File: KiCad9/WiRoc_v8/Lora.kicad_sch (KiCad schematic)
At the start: 11 parts, among them J11 Conn_01x05, J7 Conn_02x05_Odd_Even, J9 Conn_Coaxial, U8 RAK3172-xx-43-SM-xI

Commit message: etc
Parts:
- removed C18: 4.7uF, Capacitor_SMD:C_0402_1005Metric, symbol Device:C
- added C15, C21: 47uF, Capacitor_SMD:C_1206_3216Metric, symbol Device:C
- added FB1: FerriteBead, Capacitor_SMD:C_1206_3216Metric, symbol Device:FerriteBead
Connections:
- net GND: now also C15.2, C21.2
- net VDD_SYS_3.3V: now also C15.1, FB1.1; no longer U8.24 (VDD)
- new net: C21.1, FB1.2, U8.24 (VDD)
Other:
- note added: "NOTES...Ferrite bead for 1.5Mhz supply switching, 440Mhz radio: muRata BLM31PG601SN1L Or TDK MPZ2012S601AT000 https://www.youtube.com/watch?v=S6Uxx5PCRQY https://www.youtube.com/watch?v=TpXvac1Y3h0"
- moved on the sheet: R59

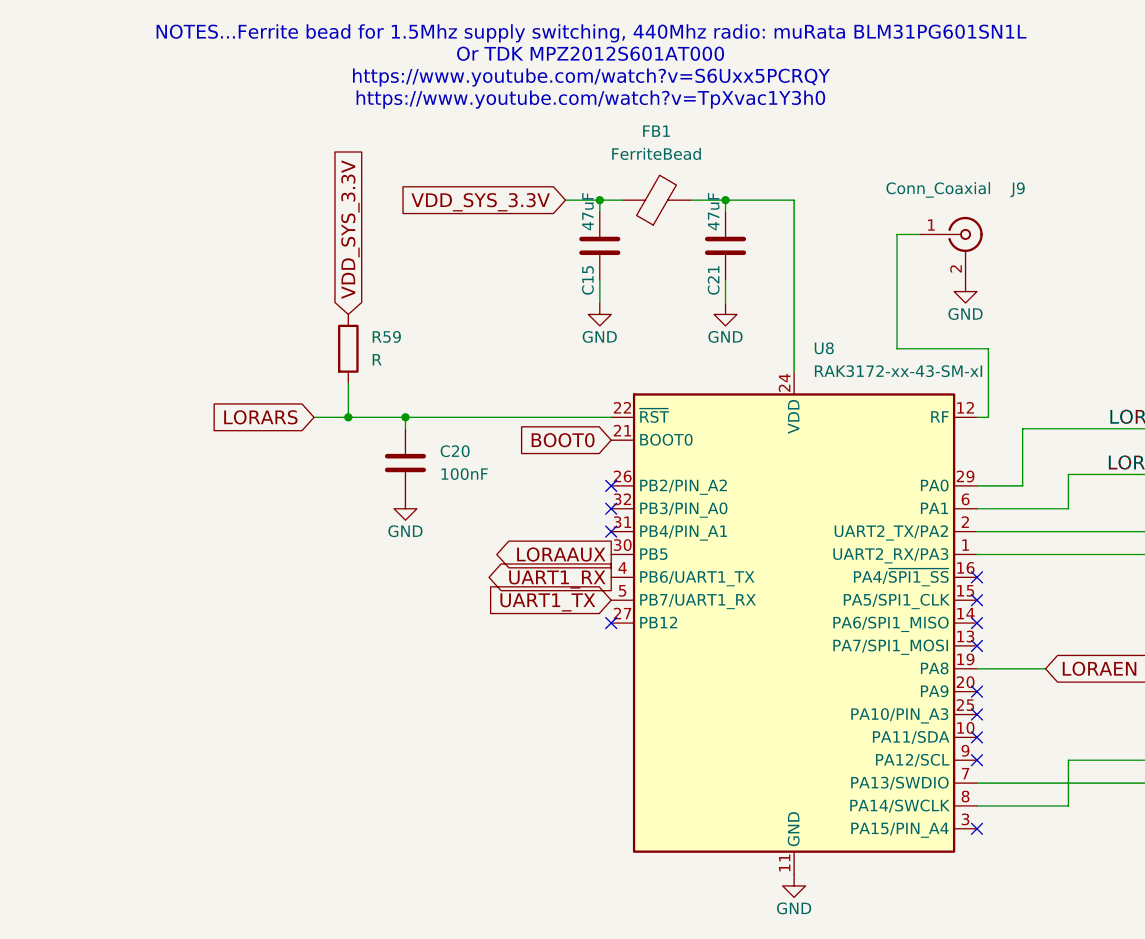
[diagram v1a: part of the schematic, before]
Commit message: add bom
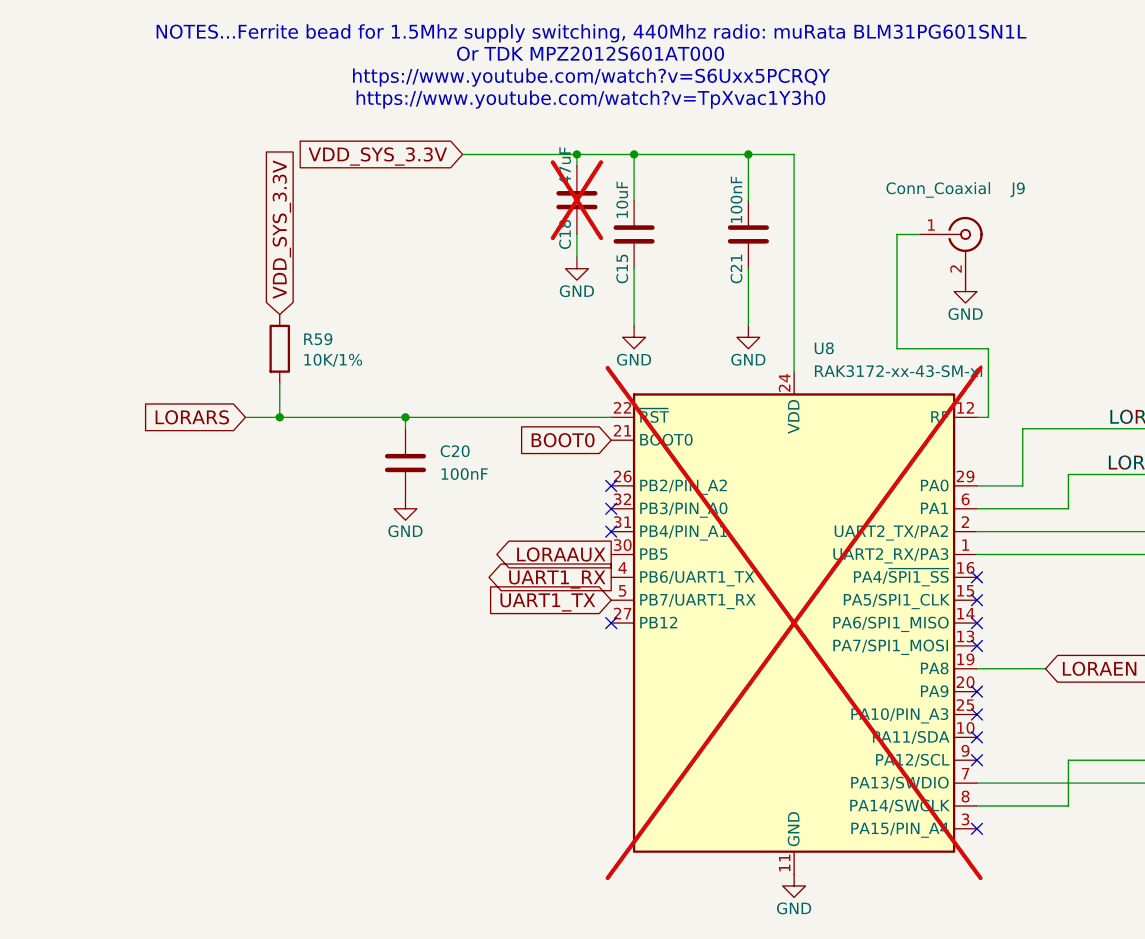
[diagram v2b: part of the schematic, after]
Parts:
- removed FB1: FerriteBead, Capacitor_SMD:C_1206_3216Metric, symbol Device:FerriteBead
- added C18: 47uF, Capacitor_SMD:C_1206_3216Metric, symbol Device:C
- C15: value 47uF -> 10uF; footprint Capacitor_SMD:C_1206_3216Metric -> Capacitor_SMD:C_0402_1005Metric; JLCBasicExtended (none) -> Basic; LCSC Part # C96123 -> C15525; Manufacturer Murata Electronics -> Samsung Electro-Mechanics; ManufacturerPartNumber CL31A476MPHNNNE -> CL05A106MQ5NUNC; Package 1206 -> 0402
- C20: IncludeInBOM (none) -> TRUE; JLCBasicExtended (none) -> Basic; LCSC Part # (none) -> C1525; Manufacturer (none) -> Samsung Electro-Mechanics; ManufacturerPartNumber (none) -> CL05B104KO5NNNC; Package (none) -> 0402
- C21: value 47uF -> 100nF; footprint Capacitor_SMD:C_1206_3216Metric -> Capacitor_SMD:C_0402_1005Metric; JLCBasicExtended (none) -> Basic; LCSC Part # C96123 -> C1525; Manufacturer Murata Electronics -> Samsung Electro-Mechanics; ManufacturerPartNumber CL31A476MPHNNNE -> CL05B104KO5NNNC; Package 1206 -> 0402
- D3: JLCBasicExtended (none) -> Extended
- J11: IncludeInBOM (none) -> FALSE; JLCBasicExtended (none) -> Extended; LCSC Part # (none) -> C6332198; Manufacturer (none) -> Hanbo Electronic; ManufacturerPartNumber (none) -> HB-PH3-25415PB2GOP
- J7: IncludeInBOM (none) -> FALSE; JLCBasicExtended (none) -> Extended; LCSC Part # (none) -> C5142394; Manufacturer (none) -> MINTRON; ManufacturerPartNumber (none) -> MTP310-1205S2
- R56, R57, R58: JLCBasicExtended (none) -> Basic; LCSC Part # C21190 -> C11702; ManufacturerPartNumber 0603WAJ0102T5E -> 0402WGF1001TCE; Package 0603 -> 0402
- R59: value R -> 10K/1%; IncludeInBOM (none) -> TRUE; JLCBasicExtended (none) -> Basic; LCSC Part # (none) -> C25744; Manufacturer (none) -> Uniroyal Elec; ManufacturerPartNumber (none) -> 0402WGF1002TCE; Package (none) -> 0402
- U8: IncludeInBOM (none) -> FALSE; now not fitted
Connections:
- net GND: now also C18.2
- net VDD_SYS_3.3V: now also C21.1, U8.24 (VDD), C18.1
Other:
- moved on the sheet: C21, R59

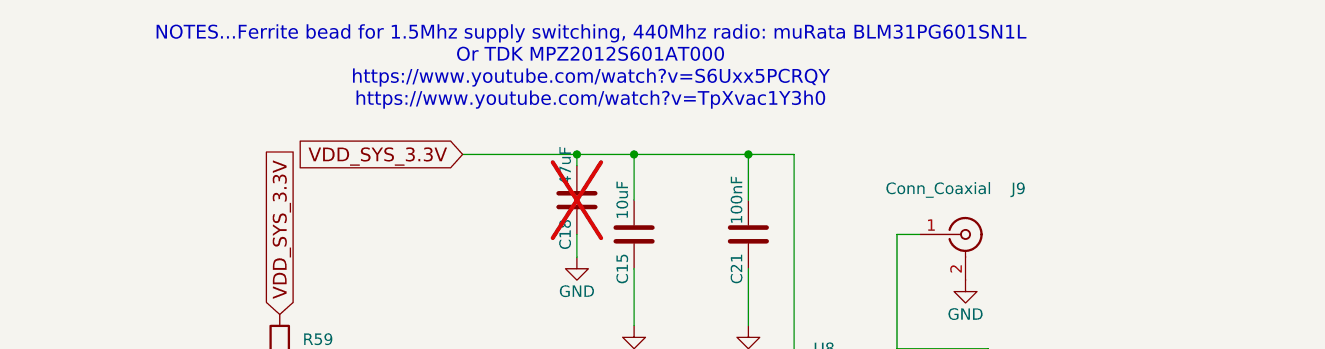
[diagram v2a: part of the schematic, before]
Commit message: change tracewidth for mem, add nettie for better length calculation
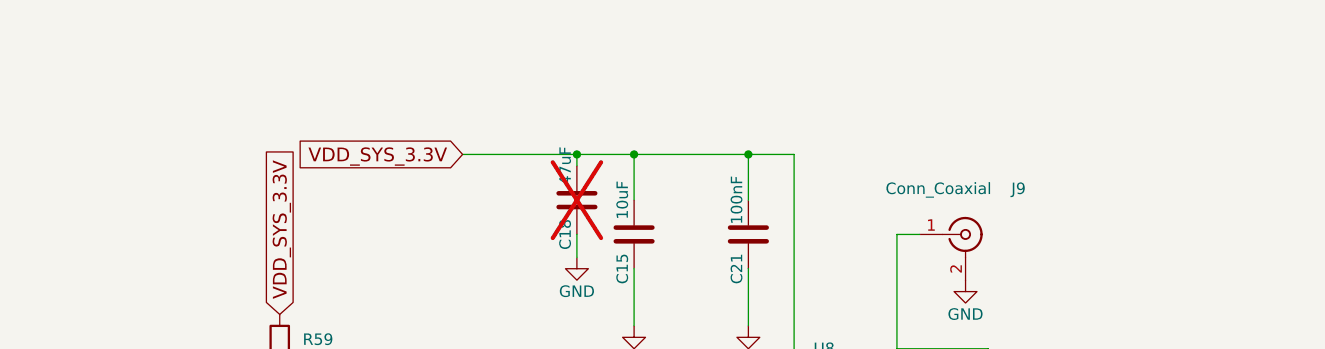
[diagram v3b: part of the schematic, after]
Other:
- note removed: "NOTES...Ferrite bead for 1.5Mhz supply switching, 440Mhz radio: muRata BLM31PG601SN1L Or TDK MPZ2012S601AT000 https://www.youtube.com/watch?v=S6Uxx5PCRQY https://www.youtube.com/watch?v=TpXvac1Y3h0"
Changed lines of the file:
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@@
 	(generator_version "9.0")
 	(paper "A4")
-	(text "NOTES...Ferrite bead for 1.5Mhz supply switching, 440Mhz radio: muRata BLM31PG601SN1L\nOr TDK MPZ2012S601AT000\nhttps://www.youtube.com/watch?v=S6Uxx5PCRQY\nhttps://www.youtube.com/watch?v=TpXvac1Y3h0"
-		(exclude_from_sim no)
-		(at 65.024 15.748 0)
-		(effects
-			(font
-				(size 1.524 1.524)
-			)
-		)
-	)
 	(text "Black magic probe connector"
 		(exclude_from_sim no)

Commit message: save point for fix to layer issues in6
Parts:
- removed C21: 100nF, Capacitor_SMD:C_0402_1005Metric, symbol Device:C
- added C34: 10uF, Capacitor_SMD:C_0402_1005Metric, symbol Device:C
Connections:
- net GND: now also C34.2
- net VDD_SYS_3.3V: now also C34.1
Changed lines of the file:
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@@
 		(on_board yes)
 		(dnp no)
-		(property "Reference" "C21"
+		(property "Reference" "C34"
 			(at 81.28 38.1 90)
 			(effects
@@
 			)
 		)
-		(property "Value" "100nF"
+		(property "Value" "10uF"
 			(at 81.28 30.48 90)
 			(effects
@@
 			)
 		)
-		(property "ManufacturerPartNumber" "CL05B104KO5NNNC"
+		(property "ManufacturerPartNumber" "CL05A106MQ5NUNC"
 			(at -186.69 104.14 0)
 			(effects
@@
 			)
 		)
-		(property "LCSC Part #" "C1525"
+		(property "LCSC Part #" "C15525"
 			(at 82.55 34.29 0)
 			(effects
@@
 			(project "WiRoc_NanoPi"
 				(path "/8ba0b499-eaca-4cd5-a002-c6bdb610cc8c/3541f406-28e2-49e9-9564-15b380efce59"
-					(reference "C21")
+					(reference "C34")
 					(unit 1)
 				)

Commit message: many small changes, change eMMC
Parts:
- C15, C34: value 10uF -> 10uF/6.3V
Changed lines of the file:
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@@
 			)
 		)
-		(property "Value" "10uF"
+		(property "Value" "10uF/6.3V"
 			(at 81.28 30.48 90)
 			(effects
@@
 			)
 		)
-		(property "Value" "10uF"
+		(property "Value" "10uF/6.3V"
 			(at 68.58 30.48 90)
 			(effects

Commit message: etc
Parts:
- C18, J11, J7, U8: now left out of the parts list
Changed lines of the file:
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@@
-			)
-		)
-		(property "JLCPCB Rotation Offset" ""
-			(at 106.68 34.29 0)
-			(effects
-				(font
-					(size 1.27 1.27)
-				)
-				(hide yes)
 			)
 		)
@@
 		)
 		(property "LCSC Part #" "C15525"
-			(at 82.55 34.29 0)
-			(effects
-				(font
-					(size 1.27 1.27)
-				)
-				(hide yes)
-			)
-		)
-		(property "JLCPCB Rotation Offset" ""
 			(at 82.55 34.29 0)
 			(effects
@@
 			)
 		)
-		(property "JLCPCB Rotation Offset" ""
-			(at 161.29 59.69 0)
-			(effects
-				(font
-					(size 1.27 1.27)
-				)
-				(hide yes)
-			)
-		)
 		(property "JLCBasicExtended" "Basic"
 			(at 161.29 59.69 90)
@@
 		(unit 1)
 		(exclude_from_sim no)
-		(in_bom yes)
+		(in_bom no)
 		(on_board yes)
 		(dnp no)
@@
 			)
 		)
-		(property "JLCPCB Rotation Offset" ""
-			(at 161.29 62.23 0)
-			(effects
-				(font
-					(size 1.27 1.27)
-				)
-				(hide yes)
-			)
-		)
 		(property "JLCBasicExtended" "Basic"
 			(at 161.29 62.23 90)
@@
 		(unit 1)
 		(exclude_from_sim no)
-		(in_bom yes)
+		(in_bom no)
 		(on_board yes)
 		(dnp yes)
@@
 			)
 		)
-		(property "JLCPCB Rotation Offset" ""
-			(at 161.29 55.88 0)
-			(effects
-				(font
-					(size 1.27 1.27)
-				)
-				(hide yes)
-			)
-		)
 		(property "JLCBasicExtended" "Basic"
 			(at 161.29 55.88 90)
@@
 		(unit 1)
 		(exclude_from_sim no)
-		(in_bom yes)
+		(in_bom no)
 		(on_board yes)
 		(dnp no)
@@
 			)
 		)
-		(property "JLCPCB Rotation Offset" ""
+		(property "JLCBasicExtended" "Extended"
 			(at 149.86 58.42 0)
 			(effects
@@
 			)
 		)
-		(property "JLCBasicExtended" "Extended"
+		(property "FT Rotation Offset" ""
 			(at 149.86 58.42 0)
 			(effects
@@
 		(unit 1)
 		(exclude_from_sim no)
-		(in_bom yes)
+		(in_bom no)
 		(on_board yes)
 		(dnp yes)
@@
 		)
 		(property "LCSC Part #" "C96123"
-			(at 63.5 30.48 0)
-			(effects
-				(font
-					(size 1.27 1.27)
-				)
-				(hide yes)
-			)
-		)
-		(property "JLCPCB Rotation Offset" ""
 			(at 63.5 30.48 0)
 			(effects
@@
 			(at 69.85 34.29 0)
 			(effects
-				(font
-					(size 1.27 1.27)
-				)
-				(hide yes)
-			)
-		)
-		(property "JLCPCB Rotation Offset" ""
-			(at 69.85 34.29 0)
-			(effects

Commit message: add ethernet etc
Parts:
- removed J7: Conn_02x05_Odd_Even, Connector_PinHeader_1.27mm:PinHeader_2x05_P1.27mm_Vertical, symbol Connector_Generic:Conn_02x05_Odd_Even
- added J1: TC2050, Connector:Tag-Connect_TC2050-IDC-NL_2x05_P1.27mm_Vertical, symbol Connector:TC2050
- added R14: 10K/1%, Resistor_SMD:R_0402_1005Metric, symbol Device:R
- added SW2: SW_SPST, Connector_PinHeader_1.27mm:PinHeader_1x02_P1.27mm_Vertical, symbol Switch:SW_SPST
- added U20: SY6280, Package_TO_SOT_SMD:SOT-23-5, symbol WiRoc:SY6280
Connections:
- net GND: now also J1.2, J1.3, R14.1, SW2.1 (A), U20.2 (GND)
- net LORAEN: now also U20.4 (EN); no longer U8.19 (PA8)
- net VDD_SYS_3.3V: now also J1.1, U20.5 (IN); no longer C15.1, C18.1, C34.1, U8.24 (VDD)
- net LORA_UART2_RX: now reaches J11.1 (Pin_1), U8.1 (UART2_RX/PA3)
- net LORA_UART2_RX: now also J1.4
- net LORA_UART2_TX: now reaches J11.2 (Pin_2), U8.2 (UART2_TX/PA2)
- net LORA_UART2_TX: now also J1.5
- net LORA-SWDIO: now reaches U8.7 (PA13/SWDIO)
- net LORA-SWDIO: now also J1.10
- net LORA-SWCLK: now reaches U8.8 (PA14/SWCLK)
- net LORA-SWCLK: now also J1.9
- net LORARS renamed LORA_RESET
- net LORA_RESET: now also J1.6, SW2.2 (B)
- new net: C15.1, C18.1, C34.1, U20.1 (OUT), U8.24 (VDD)
- new net: R14.2, U20.3 (ISET)
- new net LORAIRQ: U8.19 (PA8)
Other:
- moved on the sheet: C15, C18, C20, C34, D3, J11, J9, R56, R57, R58, R59, U8
